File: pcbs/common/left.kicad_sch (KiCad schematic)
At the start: 89 parts, among them J2 TRS

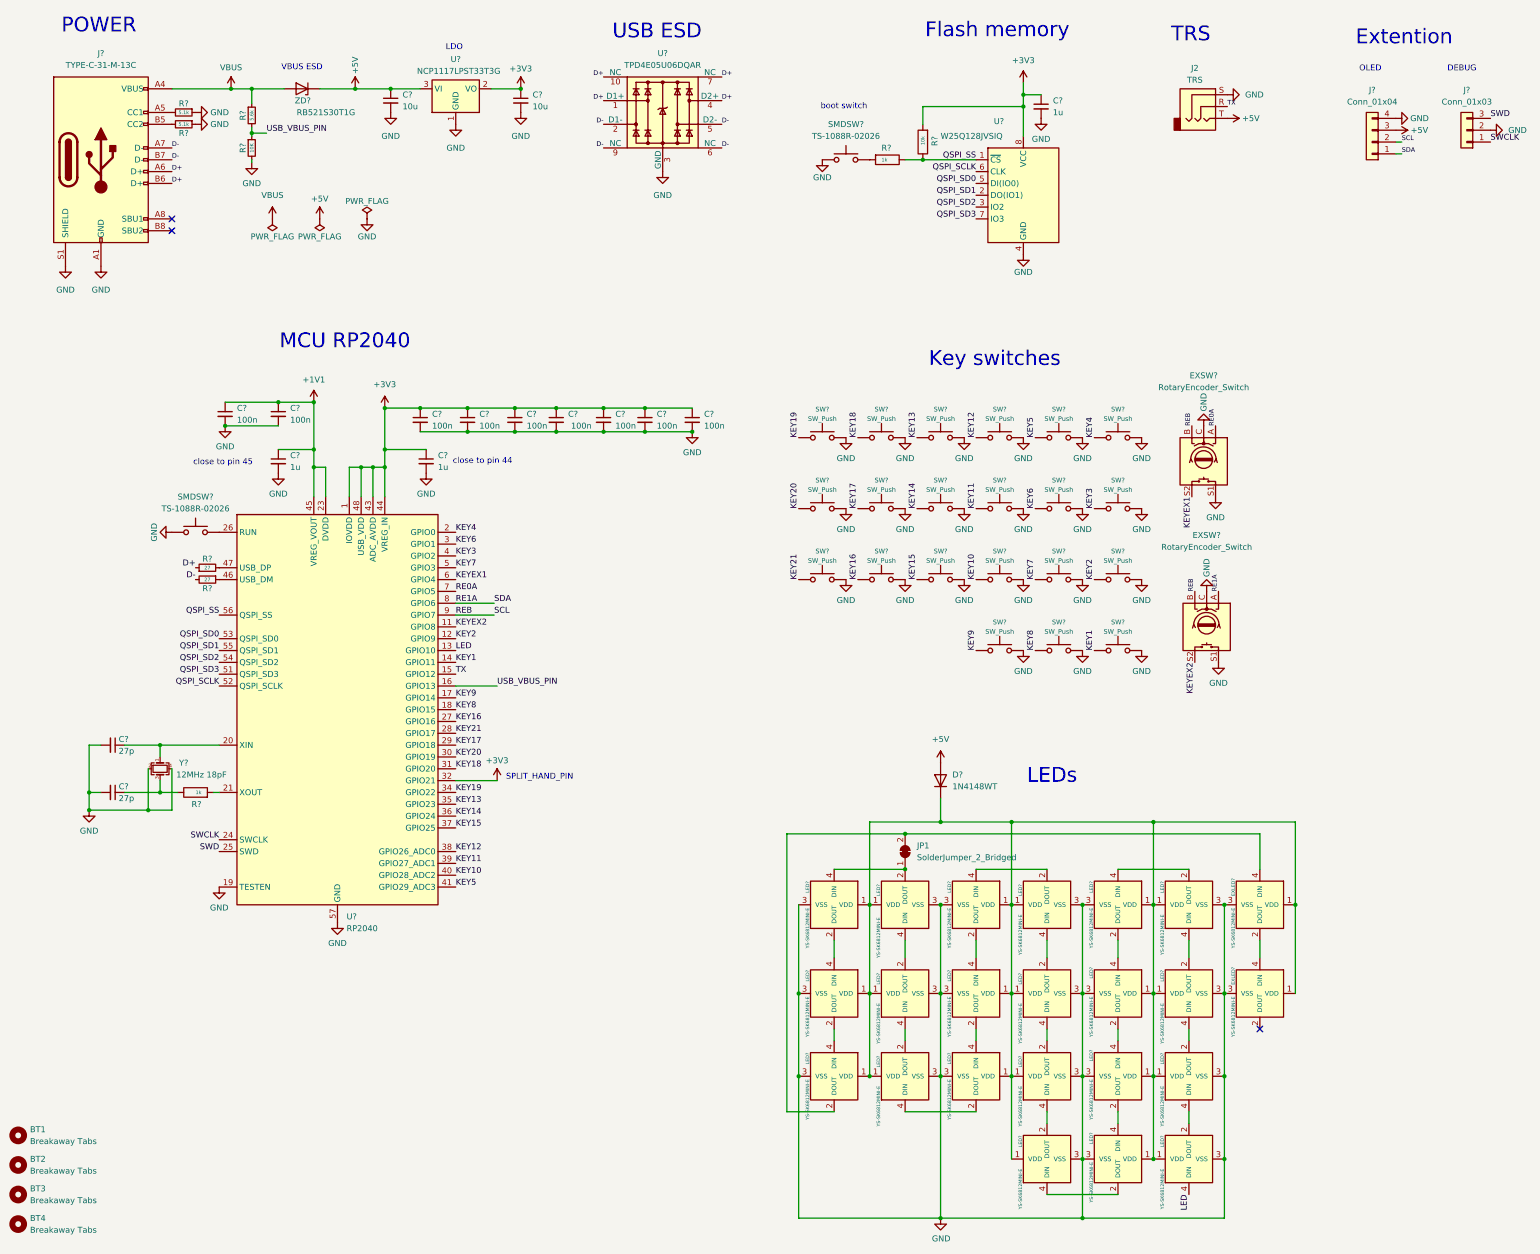
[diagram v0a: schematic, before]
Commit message: Change 4 layer left side
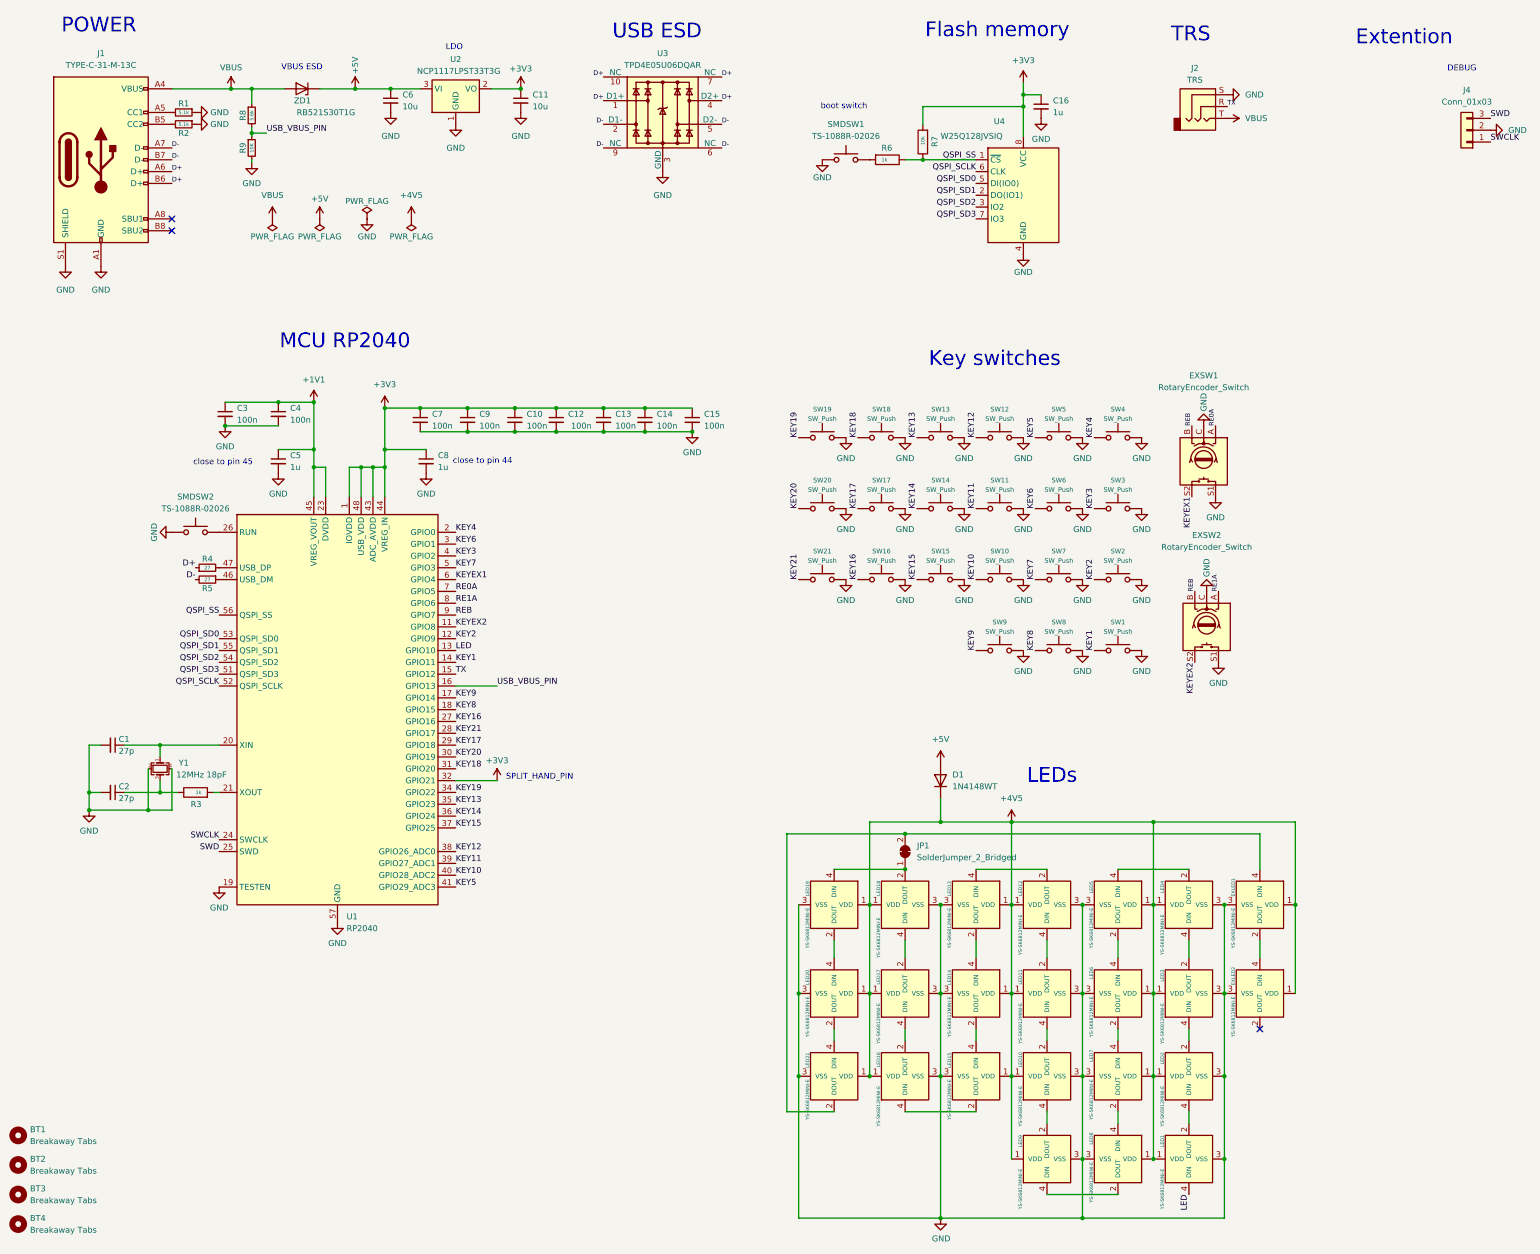
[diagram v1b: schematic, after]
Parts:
- removed J?: Conn_01x04, kbd_local:OLED, symbol Connector_Generic:Conn_01x04
- gave numbers to parts that had none: 82
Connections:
- net +5V: no longer J2.T
- net VBUS: now also J2.T
- net +4V5R: now reaches D1.1 (K), EXLED1.1 (VDD), EXLED2.1 (VDD), LED1.1 (VDD), LED10.1 (VDD), LED11.1 (VDD), LED12.1 (VDD), LED13.1 (VDD), LED14.1 (VDD), LED15.1 (VDD), LED16.1 (VDD), LED17.1 (VDD), LED18.1 (VDD), LED19.1 (VDD), LED2.1 (VDD), LED20.1 (VDD), LED21.1 (VDD), LED3.1 (VDD), LED4.1 (VDD), LED5.1 (VDD), LED6.1 (VDD), LED7.1 (VDD), LED8.1 (VDD), LED9.1 (VDD)
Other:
- note removed: "OLED"
